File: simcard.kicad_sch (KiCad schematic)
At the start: 9 parts, among them CON4 SIM_CARD

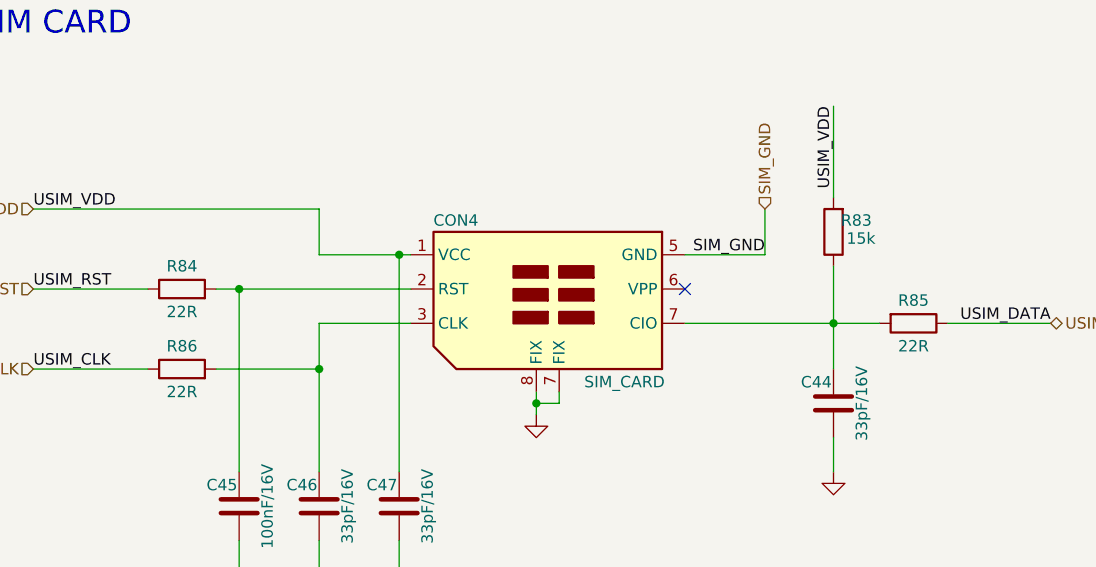
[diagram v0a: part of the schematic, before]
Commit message: Atualização das referências dos componentes
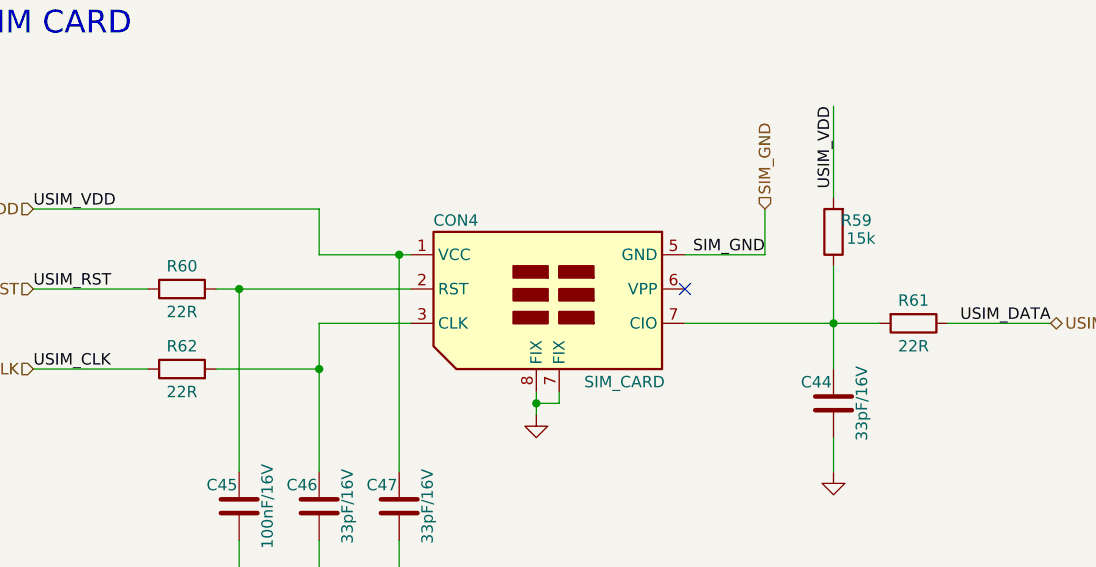
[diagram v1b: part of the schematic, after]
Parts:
- renumbered R83 to R59, R84 to R60, R85 to R61, R86 to R62
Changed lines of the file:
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@@
   (symbol (lib_id "Device:R") (at 186.69 86.36 270) (unit 1)
     (in_bom yes) (on_board yes)
-    (property "Reference" "R85" (id 0) (at 186.69 83.82 90))
+    (property "Reference" "R61" (id 0) (at 186.69 83.82 90))
     (property "Value" "22R" (id 1) (at 186.69 88.9 90))
     (property "Footprint" "Resistor_SMD:R_0603_1608Metric_Pad0.98x0.95mm_HandSolder" (id 2) (at 186.69 84.582 90)
@@
   (symbol (lib_id "power:GND") (at 177.8 102.87 0) (unit 1)
     (in_bom yes) (on_board yes) (fields_autoplaced)
-    (property "Reference" "#PWR0124" (id 0) (at 177.8 109.22 0)
+    (property "Reference" "#PWR0102" (id 0) (at 177.8 109.22 0)
       (effects (font (size 1.27 1.27)) hide)
     )
@@
   (symbol (lib_id "Device:R") (at 105.41 91.44 90) (unit 1)
     (in_bom yes) (on_board yes)
-    (property "Reference" "R86" (id 0) (at 105.41 88.9 90))
+    (property "Reference" "R62" (id 0) (at 105.41 88.9 90))
     (property "Value" "22R" (id 1) (at 105.41 93.98 90))
     (property "Footprint" "Resistor_SMD:R_0603_1608Metric_Pad0.98x0.95mm_HandSolder" (id 2) (at 105.41 93.218 90)
@@
   (symbol (lib_id "power:GND") (at 120.65 114.3 0) (unit 1)
     (in_bom yes) (on_board yes) (fields_autoplaced)
-    (property "Reference" "#PWR0126" (id 0) (at 120.65 120.65 0)
+    (property "Reference" "#PWR0104" (id 0) (at 120.65 120.65 0)
       (effects (font (size 1.27 1.27)) hide)
     )
@@
   (symbol (lib_id "power:GND") (at 144.78 96.52 0) (unit 1)
     (in_bom yes) (on_board yes) (fields_autoplaced)
-    (property "Reference" "#PWR0123" (id 0) (at 144.78 102.87 0)
+    (property "Reference" "#PWR0101" (id 0) (at 144.78 102.87 0)
       (effects (font (size 1.27 1.27)) hide)
     )
@@
   (symbol (lib_id "power:GND") (at 111.76 114.3 0) (unit 1)
     (in_bom yes) (on_board yes) (fields_autoplaced)
-    (property "Reference" "#PWR0125" (id 0) (at 111.76 120.65 0)
+    (property "Reference" "#PWR0103" (id 0) (at 111.76 120.65 0)
       (effects (font (size 1.27 1.27)) hide)
     )
@@
   (symbol (lib_id "power:GND") (at 129.54 114.3 0) (unit 1)
     (in_bom yes) (on_board yes) (fields_autoplaced)
-    (property "Reference" "#PWR0127" (id 0) (at 129.54 120.65 0)
+    (property "Reference" "#PWR0105" (id 0) (at 129.54 120.65 0)
       (effects (font (size 1.27 1.27)) hide)
     )
@@
   (symbol (lib_id "Device:R") (at 177.8 76.2 180) (unit 1)
     (in_bom yes) (on_board yes)
-    (property "Reference" "R83" (id 0) (at 180.34 74.93 0))
+    (property "Reference" "R59" (id 0) (at 180.34 74.93 0))
     (property "Value" "15k" (id 1) (at 180.8513 76.9331 0))
     (property "Footprint" "Resistor_SMD:R_0603_1608Metric_Pad0.98x0.95mm_HandSolder" (id 2) (at 179.578 76.2 90)
@@
   (symbol (lib_id "Device:R") (at 105.41 82.55 90) (unit 1)
     (in_bom yes) (on_board yes)
-    (property "Reference" "R84" (id 0) (at 105.41 80.01 90))
+    (property "Reference" "R60" (id 0) (at 105.41 80.01 90))
     (property "Value" "22R" (id 1) (at 105.41 85.09 90))
     (property "Footprint" "Resistor_SMD:R_0603_1608Metric_Pad0.98x0.95mm_HandSolder" (id 2) (at 105.41 84.328 90)

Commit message: Inserido as informações dos sheets do modulo IoT
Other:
- company: (none) -> Magalhaes
- title: (none) -> SIM Card
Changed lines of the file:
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@@
 (kicad_sch (version 20211123) (generator eeschema)
   (paper "A4")
+  (title_block
+    (title "SIM Card")
+    (date "2022-08-10")
+    (rev "0.0.0")
+    (company "Magalhaes")
+    (comment 1 "Author: Alexandre Magalhães")
+    (comment 2 "Variant 1: Full")
+  )
   (junction (at 129.54 78.74) (diameter 0) (color 0 0 0 0)
   )

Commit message: Referencia dos componentes
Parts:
- renumbered R59 to R61, R60 to R62, R61 to R63, R62 to R64
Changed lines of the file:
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@@
   (symbol (lib_id "Device:R") (at 186.69 86.36 270) (unit 1)
     (in_bom yes) (on_board yes)
-    (property "Reference" "R61" (id 0) (at 186.69 83.82 90))
+    (property "Reference" "R63" (id 0) (at 186.69 83.82 90))
     (property "Value" "22R" (id 1) (at 186.69 88.9 90))
     (property "Footprint" "Resistor_SMD:R_0603_1608Metric_Pad0.98x0.95mm_HandSolder" (id 2) (at 186.69 84.582 90)
@@
   (symbol (lib_id "power:GND") (at 177.8 102.87 0) (unit 1)
     (in_bom yes) (on_board yes) (fields_autoplaced)
-    (property "Reference" "#PWR0102" (id 0) (at 177.8 109.22 0)
+    (property "Reference" "#PWR0103" (id 0) (at 177.8 109.22 0)
       (effects (font (size 1.27 1.27)) hide)
     )
@@
   (symbol (lib_id "Device:R") (at 105.41 91.44 90) (unit 1)
     (in_bom yes) (on_board yes)
-    (property "Reference" "R62" (id 0) (at 105.41 88.9 90))
+    (property "Reference" "R64" (id 0) (at 105.41 88.9 90))
     (property "Value" "22R" (id 1) (at 105.41 93.98 90))
     (property "Footprint" "Resistor_SMD:R_0603_1608Metric_Pad0.98x0.95mm_HandSolder" (id 2) (at 105.41 93.218 90)
@@
   (symbol (lib_id "power:GND") (at 120.65 114.3 0) (unit 1)
     (in_bom yes) (on_board yes) (fields_autoplaced)
-    (property "Reference" "#PWR0104" (id 0) (at 120.65 120.65 0)
+    (property "Reference" "#PWR0105" (id 0) (at 120.65 120.65 0)
       (effects (font (size 1.27 1.27)) hide)
     )
@@
   (symbol (lib_id "power:GND") (at 144.78 96.52 0) (unit 1)
     (in_bom yes) (on_board yes) (fields_autoplaced)
-    (property "Reference" "#PWR0101" (id 0) (at 144.78 102.87 0)
+    (property "Reference" "#PWR0102" (id 0) (at 144.78 102.87 0)
       (effects (font (size 1.27 1.27)) hide)
     )
@@
   (symbol (lib_id "power:GND") (at 111.76 114.3 0) (unit 1)
     (in_bom yes) (on_board yes) (fields_autoplaced)
-    (property "Reference" "#PWR0103" (id 0) (at 111.76 120.65 0)
+    (property "Reference" "#PWR0104" (id 0) (at 111.76 120.65 0)
       (effects (font (size 1.27 1.27)) hide)
     )
@@
   (symbol (lib_id "power:GND") (at 129.54 114.3 0) (unit 1)
     (in_bom yes) (on_board yes) (fields_autoplaced)
-    (property "Reference" "#PWR0105" (id 0) (at 129.54 120.65 0)
+    (property "Reference" "#PWR0106" (id 0) (at 129.54 120.65 0)
       (effects (font (size 1.27 1.27)) hide)
     )
@@
   (symbol (lib_id "Device:R") (at 177.8 76.2 180) (unit 1)
     (in_bom yes) (on_board yes)
-    (property "Reference" "R59" (id 0) (at 180.34 74.93 0))
+    (property "Reference" "R61" (id 0) (at 180.34 74.93 0))
     (property "Value" "15k" (id 1) (at 180.8513 76.9331 0))
     (property "Footprint" "Resistor_SMD:R_0603_1608Metric_Pad0.98x0.95mm_HandSolder" (id 2) (at 179.578 76.2 90)
@@
   (symbol (lib_id "Device:R") (at 105.41 82.55 90) (unit 1)
     (in_bom yes) (on_board yes)
-    (property "Reference" "R60" (id 0) (at 105.41 80.01 90))
+    (property "Reference" "R62" (id 0) (at 105.41 80.01 90))
     (property "Value" "22R" (id 1) (at 105.41 85.09 90))
     (property "Footprint" "Resistor_SMD:R_0603_1608Metric_Pad0.98x0.95mm_HandSolder" (id 2) (at 105.41 84.328 90)

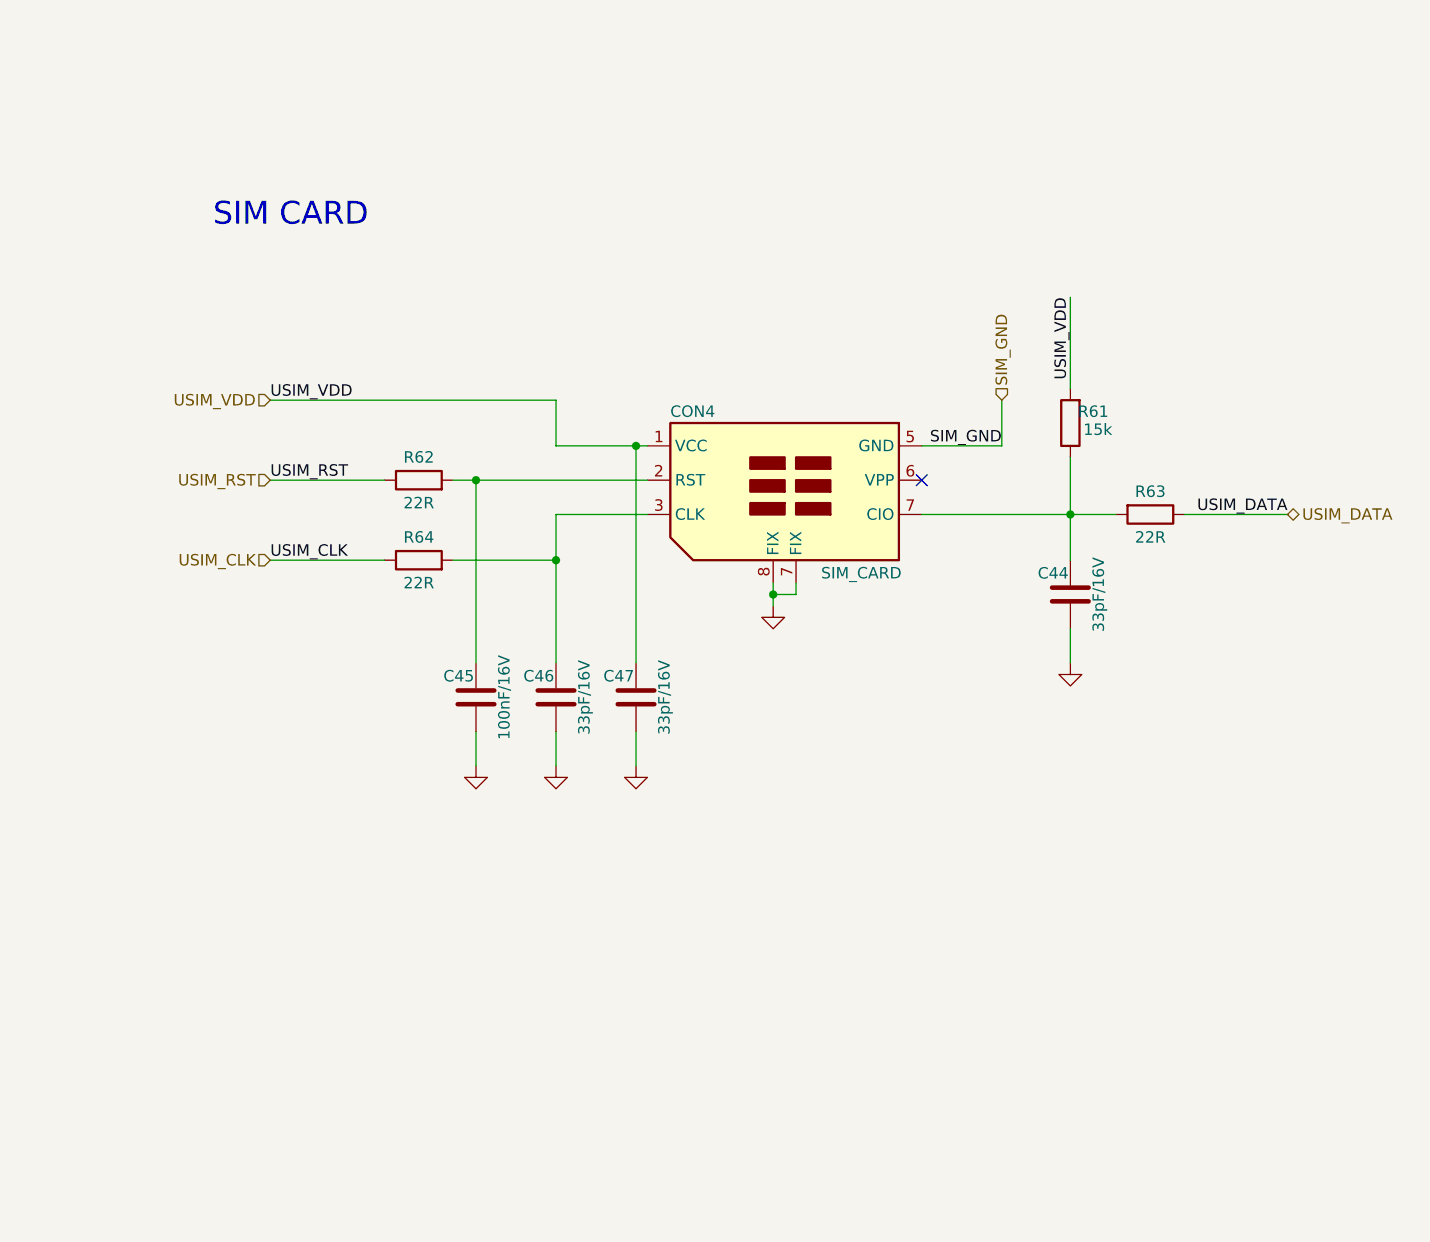
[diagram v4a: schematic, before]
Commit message: Inserido proteção ESD no SIM Card
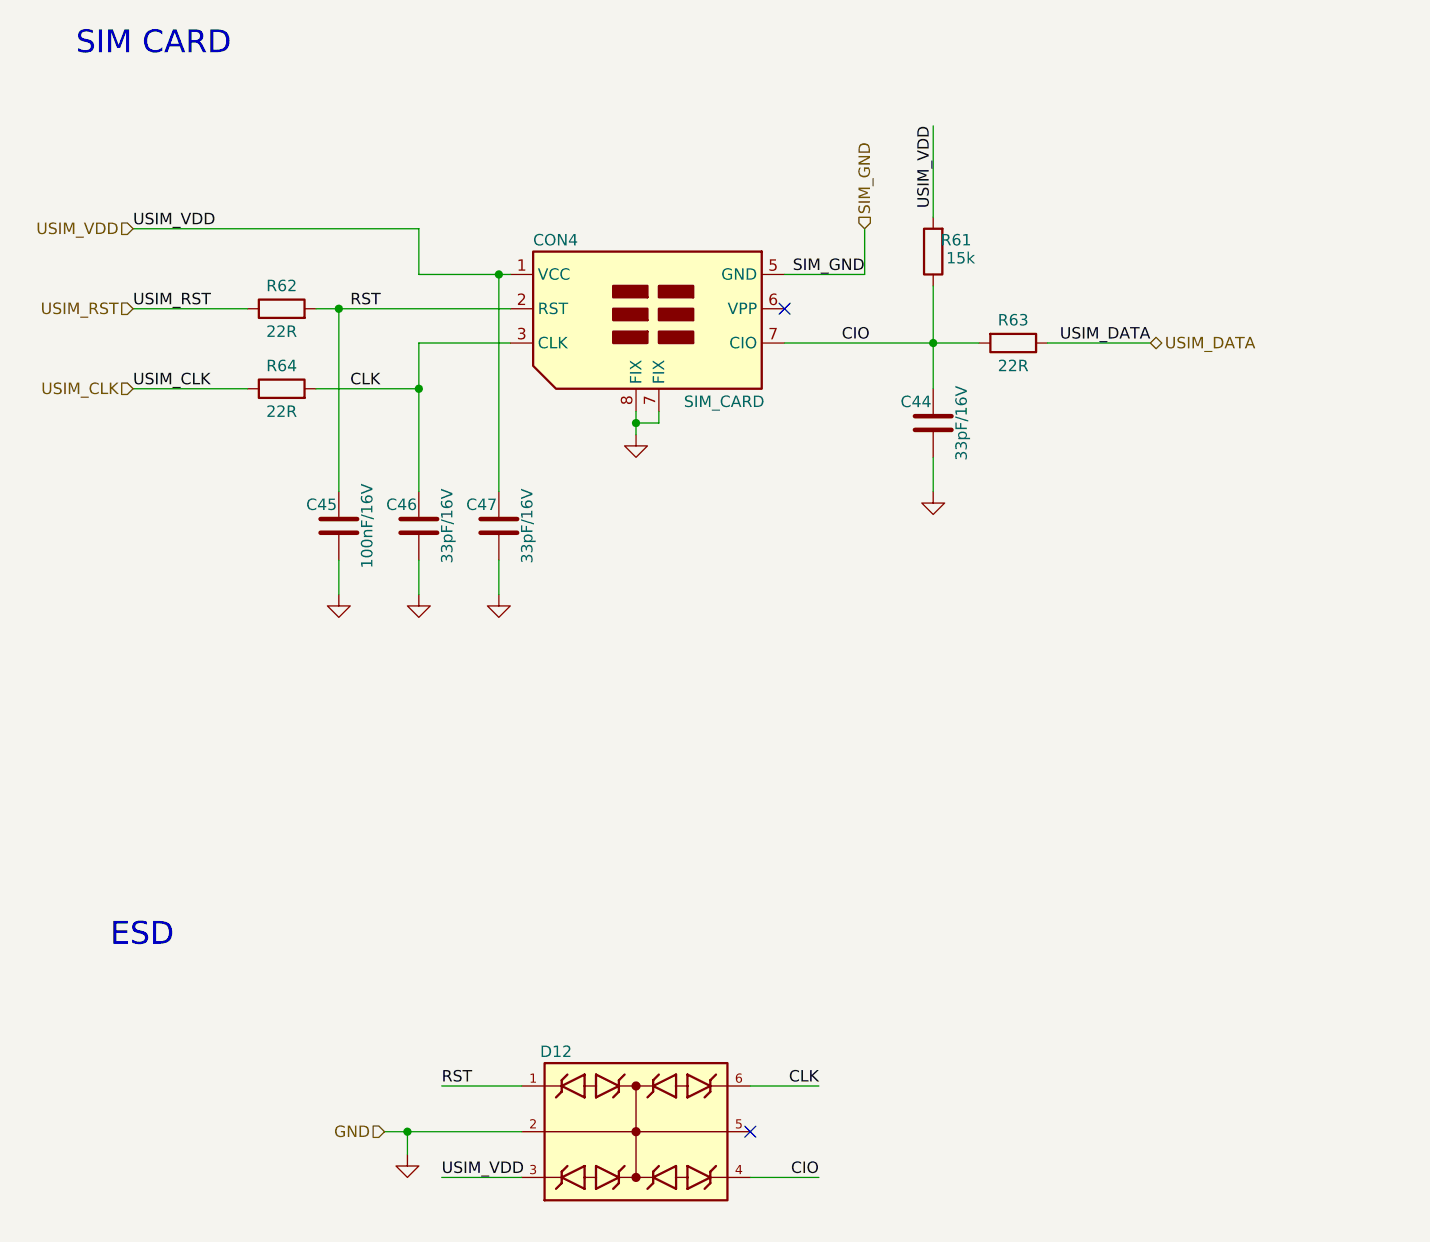
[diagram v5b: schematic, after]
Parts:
- added D12: (no value), symbol Alexandre_Library:ESDA6V1BC6
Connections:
- net GND: now also D12.2
- net USIM_VDD: now also D12.3
- net RST: now reaches C45.2, CON4.2 (RST), R62.2
- net RST: now also D12.1
- net CLK: now reaches C46.2, CON4.3 (CLK), R64.2
- net CLK: now also D12.6
- net CIO: now reaches C44.2, CON4.7 (FIX), R61.1, R63.2
- net CIO: now also D12.4
- no-connect marks 1 -> 2
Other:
- note added: "ESD"
- moved on the sheet: C44, C45, C46, C47, CON4, R61, R62, R63, R64
